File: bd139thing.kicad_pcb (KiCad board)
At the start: 2 copper layers, 75 x 75 mm, 26 parts, among them J1 Audio-Jack-3, J2 Jack-DC, Q1 PN2222, Q2 BD13916, Q3 BD13916, Q4 PN2222, Q5 BD13916, Q6 BD13916

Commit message: correct problems thx ok r5p2
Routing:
- net GND: track 182.0 -> 141.4 mm
- net +12V: track 159.0 -> 151.2 mm
- net Net-(C1-Pad1): track 58.7 -> 54.3 mm
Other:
- board text added: "BD139 Thing ver. r5p2"
- board text removed: "BD139 Thing ver. r5p1"
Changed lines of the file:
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@@
   (general
     (links 58)
-    (no_connects 3)
-    (area 29.924999 19.924999 105.075001 95.075001)
+    (no_connects 0)
+    (area 17.650001 12.639345 105.831818 95.100001)
     (thickness 1.6)
     (drawings 15)
-    (tracks 185)
+    (tracks 182)
     (zones 0)
     (modules 26)
@@
     (pcbplotparams
       (layerselection 0x010f0_80000001)
-      (usegerberextensions false)
+      (usegerberextensions true)
       (excludeedgelayer true)
       (linewidth 0.100000)
@@
       (net 3 +12V))
   )
-  (gr_text "BD139 Thing\nver. r5p1" (at 65 57.5) (layer F.SilkS)
+  (gr_text "BD139 Thing\nver. r5p2" (at 65 57.5) (layer F.SilkS)
     (effects (font (size 1.5 1.5) (thickness 0.3)))
   )
@@
     (arrow2b (pts (xy 29.842298 15.339345) (xy 30.968802 14.752924)))
   )
+  (segment (start 95 77.5) (end 92.5 75) (width 0.2) (layer F.Cu) (net 1))
+  (segment (start 92.5 75) (end 92.5 65) (width 0.2) (layer F.Cu) (net 1))
+  (segment (start 92.5 65) (end 95.30001 62.19999) (width 0.2) (layer F.Cu) (net 1))
+  (segment (start 95.30001 62.19999) (end 95.30001 57.19999) (width 0.2) (layer F.Cu) (net 1))
+  (segment (start 95.30001 57.19999) (end 95.30001 35.64739) (width 0.2) (layer F.Cu) (net 1))
+  (segment (start 95.30001 35.64739) (end 99.9854 30.962) (width 0.2) (layer F.Cu) (net 1))
+  (segment (start 99.9854 30.962) (end 99.9854 30) (width 0.2) (layer F.Cu) (net 1))
   (segment (start 99.9854 30) (end 99.9854 30.962) (width 0.2) (layer B.Cu) (net 1))
   (segment (start 95 76.646) (end 95 77.5) (width 0.2) (layer B.Cu) (net 1))
-  (segment (start 99.9854 30.962) (end 102.5 33.4766) (width 0.2) (layer B.Cu) (net 1))
-  (segment (start 92.5 74.146) (end 95 76.646) (width 0.2) (layer B.Cu) (net 1))
-  (segment (start 102.5 33.4766) (end 102.5 64.584) (width 0.2) (layer B.Cu) (net 1))
-  (segment (start 102.5 64.584) (end 102.084 65) (width 0.2) (layer B.Cu) (net 1))
-  (segment (start 102.084 65) (end 95 65) (width 0.2) (layer B.Cu) (net 1))
-  (segment (start 92.5 67.5) (end 92.5 74.146) (width 0.2) (layer B.Cu) (net 1))
-  (segment (start 95 65) (end 92.5 67.5) (width 0.2) (layer B.Cu) (net 1))
   (segment (start 95 76.646) (end 95 77.5) (width 0.2) (layer F.Cu) (net 1))
   (segment (start 62.58574 40) (end 59.99748 40) (width 0.2) (layer F.Cu) (net 2))
@@
   (segment (start 102.5 30) (end 101.487199 28.987199) (width 0.2) (layer F.Cu) (net 2))
   (segment (start 101.487199 28.987199) (end 101.487199 28.487199) (width 0.2) (layer F.Cu) (net 2))
+  (segment (start 100 42.5) (end 100 39.99748) (width 0.2) (layer B.Cu) (net 3))
+  (segment (start 92.5 50) (end 100 42.5) (width 0.2) (layer B.Cu) (net 3))
+  (segment (start 85.19697 50) (end 92.5 50) (width 0.2) (layer B.Cu) (net 3))
+  (segment (start 80.99748 53) (end 82.19697 53) (width 0.2) (layer B.Cu) (net 3))
+  (segment (start 82.19697 53) (end 85.19697 50) (width 0.2) (layer B.Cu) (net 3))
+  (segment (start 100 41.19697) (end 100 39.99748) (width 0.2) (layer F.Cu) (net 3))
   (segment (start 83.58574 62) (end 80.99748 62) (width 0.2) (layer F.Cu) (net 3))
   (segment (start 80.99748 53) (end 83.58574 53) (width 0.2) (layer F.Cu) (net 3))
@@
   (segment (start 74.46 46) (end 74.46 53.04) (width 0.2) (layer F.Cu) (net 3))
   (segment (start 74.46 53.04) (end 70 57.5) (width 0.2) (layer F.Cu) (net 3))
-  (segment (start 100 39.99748) (end 100 41.19697) (width 0.2) (layer F.Cu) (net 3))
-  (segment (start 100 41.19697) (end 95 46.19697) (width 0.2) (layer F.Cu) (net 3))
-  (segment (start 95 46.19697) (end 95 54) (width 0.2) (layer F.Cu) (net 3))
-  (segment (start 95 54) (end 91.5 57.5) (width 0.2) (layer F.Cu) (net 3))
-  (segment (start 91.5 57.5) (end 77.69697 57.5) (width 0.2) (layer F.Cu) (net 3))
   (segment (start 77.69697 57.5) (end 80.99748 60.80051) (width 0.2) (layer F.Cu) (net 3))
   (segment (start 80.99748 60.80051) (end 80.99748 62) (width 0.2) (layer F.Cu) (net 3))
@@
   (segment (start 37 69.6) (end 36.4 69) (width 0.2) (layer F.Cu) (net 7))
   (segment (start 36.4 69) (end 35 69) (width 0.2) (layer F.Cu) (net 7))
-  (segment (start 103.300001 68.545999) (end 100 71.846) (width 0.2) (layer B.Cu) (net 8))
-  (segment (start 93.388 30) (end 93.388 54.488) (width 0.2) (layer B.Cu) (net 8))
-  (segment (start 93.388 54.488) (end 98.9 60) (width 0.2) (layer B.Cu) (net 8))
   (segment (start 98.9 60) (end 100 60) (width 0.2) (layer B.Cu) (net 8))
   (segment (start 97.5 77.5) (end 100 75) (width 0.2) (layer F.Cu) (net 8))
@@
   (segment (start 100 71.846) (end 100 72.5) (width 0.2) (layer F.Cu) (net 8))
   (segment (start 100 71.846) (end 100 72.5) (width 0.2) (layer B.Cu) (net 8))
-  (segment (start 95.96 32.572) (end 93.388 30) (width 0.2) (layer B.Cu) (net 8))
   (segment (start 37.5 57.5) (end 38.825 57.5) (width 0.2) (layer B.Cu) (net 8))
   (segment (start 38.825 57.5) (end 42.325 54) (width 0.2) (layer B.Cu) (net 8))

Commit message: 6 ok
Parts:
- moved C3 109.8 mm to (7.50, 30.0)
- moved J1 109.8 mm to (5.00, 17.5), turned to 0 degrees
- moved C1 95.5 mm to (7.50, 40.0)
- moved D1 95.5 mm to (5.00, 50.0)
- moved R11 85.0 mm to (15.0, 45.0), turned to 270 degrees
- moved LS2 73.8 mm to (95.0, 26.0), turned to 90 degrees
- moved R10 72.5 mm to (93.9, 12.5)
- moved R9 68.9 mm to (25.0, 30.0)
- moved C4 62.7 mm to (30.0, 12.5)
- moved Q6 62.1 mm to (40.0, 25.1), turned to 90 degrees
- moved R4 61.5 mm to (25.0, 45.0)
- moved LS1 61.0 mm to (95.0, 53.5), turned to 90 degrees
- moved R7 54.8 mm to (25.0, 25.0)
- moved Q4 53.2 mm to (27.5, 35.0)
- moved R6 50.5 mm to (82.5, 27.6), turned to 270 degrees
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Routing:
- net GND: track 141.4 -> 46.5 mm
- net Net-(Q4-Pad1): track 17.1 -> 89.8 mm
- net Net-(C4-Pad2): track 26.2 -> 75.9 mm
- net Net-(C2-Pad2): track 21.6 -> 70.9 mm
- net Net-(Q1-Pad1): track 36.6 -> 80.2 mm
- net Net-(Q1-Pad3): track 41.9 -> 84.6 mm
- net Net-(C3-Pad2): track 56.3 -> 86.3 mm
- net Net-(Q4-Pad3): track 46.8 -> 73.6 mm
- net +12V: track 151.2 -> 124.8 mm
- net Net-(C1-Pad1): track 54.3 -> 30.8 mm
- net Net-(C1-Pad2): track 58.6 -> 81.2 mm
- net Net-(LS1-Pad2): track 90.5 -> 76.4 mm
- net Net-(LS2-Pad2): track 92.8 -> 81.4 mm
- net Net-(C3-Pad1): track 19.6 -> 9.96 mm
- net Net-(Q2-Pad1): track 16.9 -> 9.47 mm
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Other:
- board size 75 x 75 mm -> 100 x 75 mm
- net class Power added: clearance 0.25, trace_width 0.5, via_dia 0.75, via_drill 0.7
- board text added: "BD139 Thing v6.0"
- board text added: "L+"
- board text added: "L-"
- board text added: "R+"
- board text added: "R-"
- board text removed: "BD139 Thing ver. r5p2"

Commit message: ahgod if you know what happened you wouldn't be happy
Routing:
- net Net-(Q1-Pad3): track 84.6 -> 79.6 mm
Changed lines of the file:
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@@
     (links 58)
     (no_connects 0)
-    (area -12.849999 -7.7 102.125 75.100001)
+    (area -12.849999 -7.7 104.85 75.100001)
     (thickness 1.6)
     (drawings 30)
-    (tracks 184)
+    (tracks 183)
     (zones 0)
     (modules 26)
@@
     (arrow2b (pts (xy 45 -2) (xy 46.126504 -2.586421)))
   )
-  (gr_text "BD139 Thing v6.0" (at 80 71 360) (layer F.SilkS)
+  (gr_text "BD139 Thing v6.0" (at 80 71) (layer F.SilkS)
     (effects (font (size 1.5 1.5) (thickness 0.3)))
   )
@@
   (segment (start 40.528001 53.560001) (end 41.100001 52.988001) (width 0.2) (layer B.Cu) (net 11))
   (segment (start 39.279997 53.560001) (end 40.528001 53.560001) (width 0.2) (layer B.Cu) (net 11))
-  (segment (start 82.5 52.5) (end 82.5 57.5) (width 0.2) (layer F.Cu) (net 11))
   (segment (start 40 49.92) (end 30.08 49.92) (width 0.2) (layer B.Cu) (net 11))
   (segment (start 30.08 49.92) (end 30 50) (width 0.2) (layer B.Cu) (net 11))

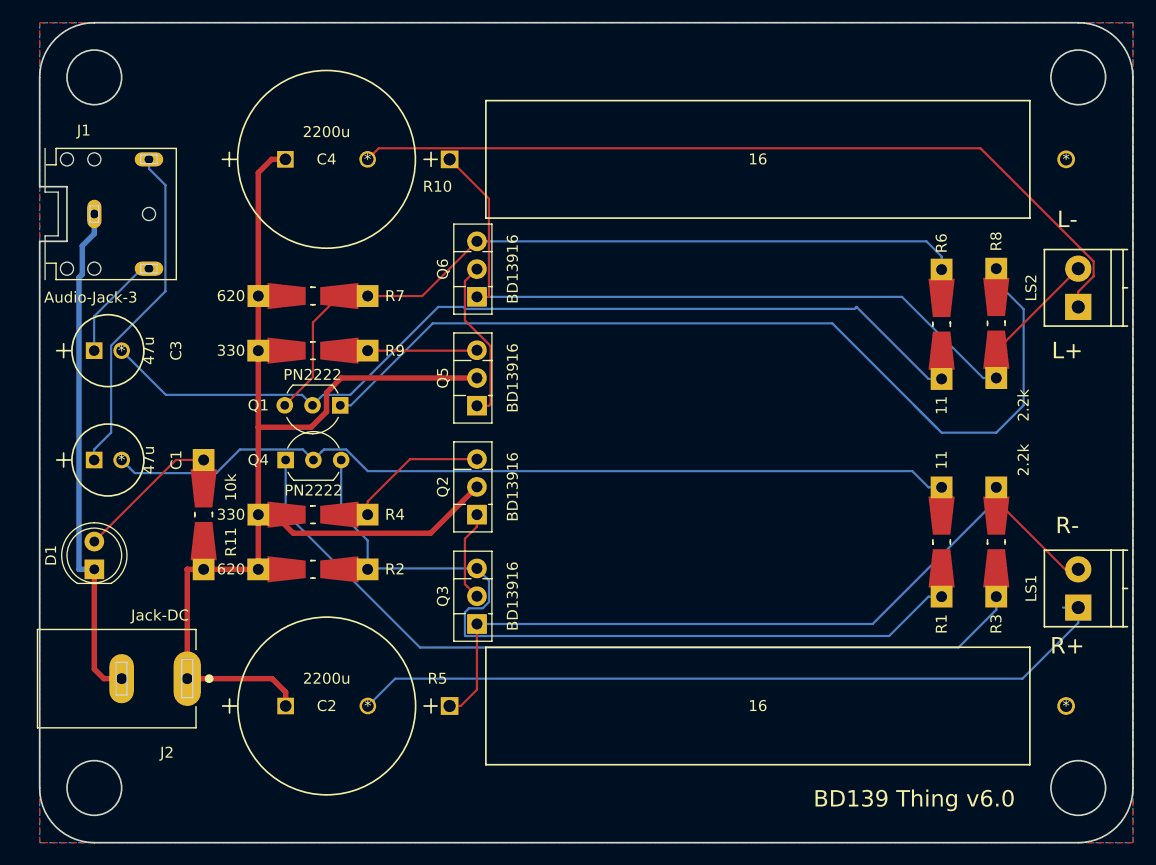
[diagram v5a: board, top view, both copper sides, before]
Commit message: design wasn't performing as planned
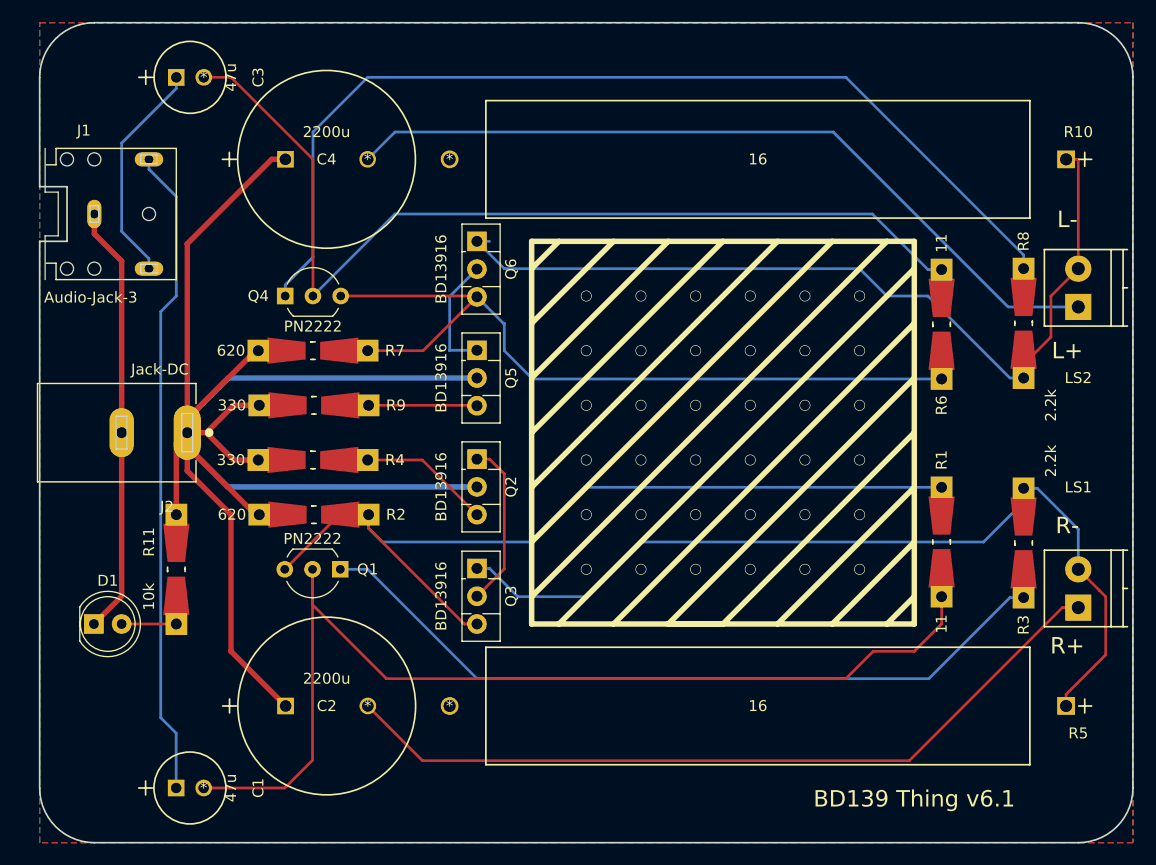
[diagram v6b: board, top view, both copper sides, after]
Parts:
- moved R10 56.4 mm to (37.5, 12.5), turned to 180 degrees
- moved R5 56.4 mm to (37.5, 62.5), turned to 180 degrees
- moved C1 30.9 mm to (15.0, 70.0)
- moved C3 26.1 mm to (15.0, 5.00)
- moved J2 22.5 mm to (13.5, 37.5)
- moved Q4 11.2 mm to (22.5, 25.0), turned to 0 degrees
- moved Q1 11.2 mm to (27.5, 50.0), turned to 180 degrees
- moved R11 5.59 mm to (12.5, 50.0), turned to 90 degrees
- moved Q2 5.08 mm to (40.0, 39.9), turned to 270 degrees
- moved Q3 5.08 mm to (40.0, 49.9), turned to 270 degrees
- moved Q5 5.08 mm to (40.0, 30.0), turned to 270 degrees
- moved Q6 5.08 mm to (40.0, 20.0), turned to 270 degrees
- moved R2 5.00 mm to (25.1, 45.0)
- moved R9 5.00 mm to (25.1, 35.0)
- moved D1 5.00 mm to (4.96, 55.0), turned to 0 degrees
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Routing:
- net +12V: track 124.8 -> 171.8 mm
- net Net-(C1-Pad1): track 30.8 -> 59.7 mm
- net Net-(C1-Pad2): track 81.2 -> 99.2 mm
- net Net-(C3-Pad1): track 9.96 -> 20.6 mm
- net Net-(D1-Pad2): track 15.7 -> 7.59 mm
- net Net-(Q1-Pad1): track 80.2 -> 72.3 mm
- net Net-(LS1-Pad2): track 76.4 -> 83.7 mm
- net GND: track 46.5 -> 39.6 mm
- net Net-(Q2-Pad1): track 9.47 -> 15.3 mm
- net Net-(C3-Pad2): track 86.3 -> 90.9 mm
- net Net-(Q5-Pad1): track 15.1 -> 11.0 mm
- net Net-(Q4-Pad1): track 89.8 -> 93.7 mm
- net Net-(Q1-Pad3): track 79.6 -> 83.4 mm
- net Net-(Q4-Pad3): track 73.6 -> 76.8 mm
- net Net-(C4-Pad2): track 75.9 -> 72.7 mm
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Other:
- outline, holes or cut-outs redrawn
- net class Default: clearance 0.1 -> 0.25; trace_width 0.2 -> 0.25; via_dia 0.45 -> 0.5; via_drill 0.4 -> 0.45
- rule trace_clearance: 0.1 -> 0.25
- board text added: "BD139 Thing v6.1"
- board text removed: "BD139 Thing v6.0"
